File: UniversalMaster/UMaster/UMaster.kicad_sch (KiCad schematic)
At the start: 1 part, among them U1 PIC16F1789

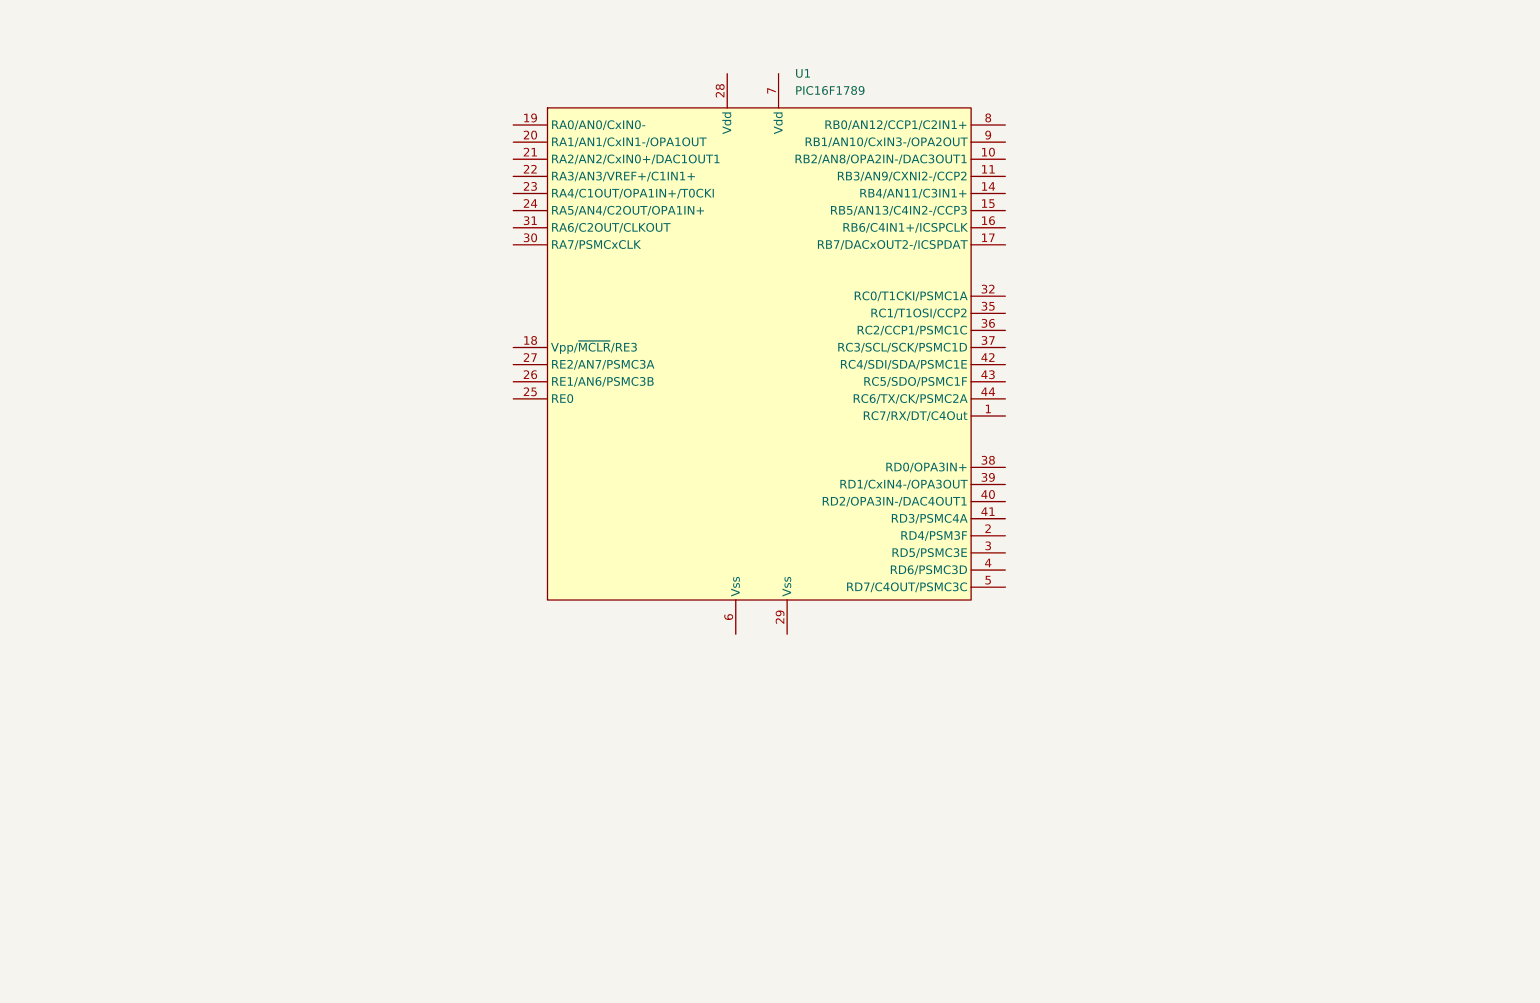
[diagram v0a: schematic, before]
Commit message: updated Universal Master schematic
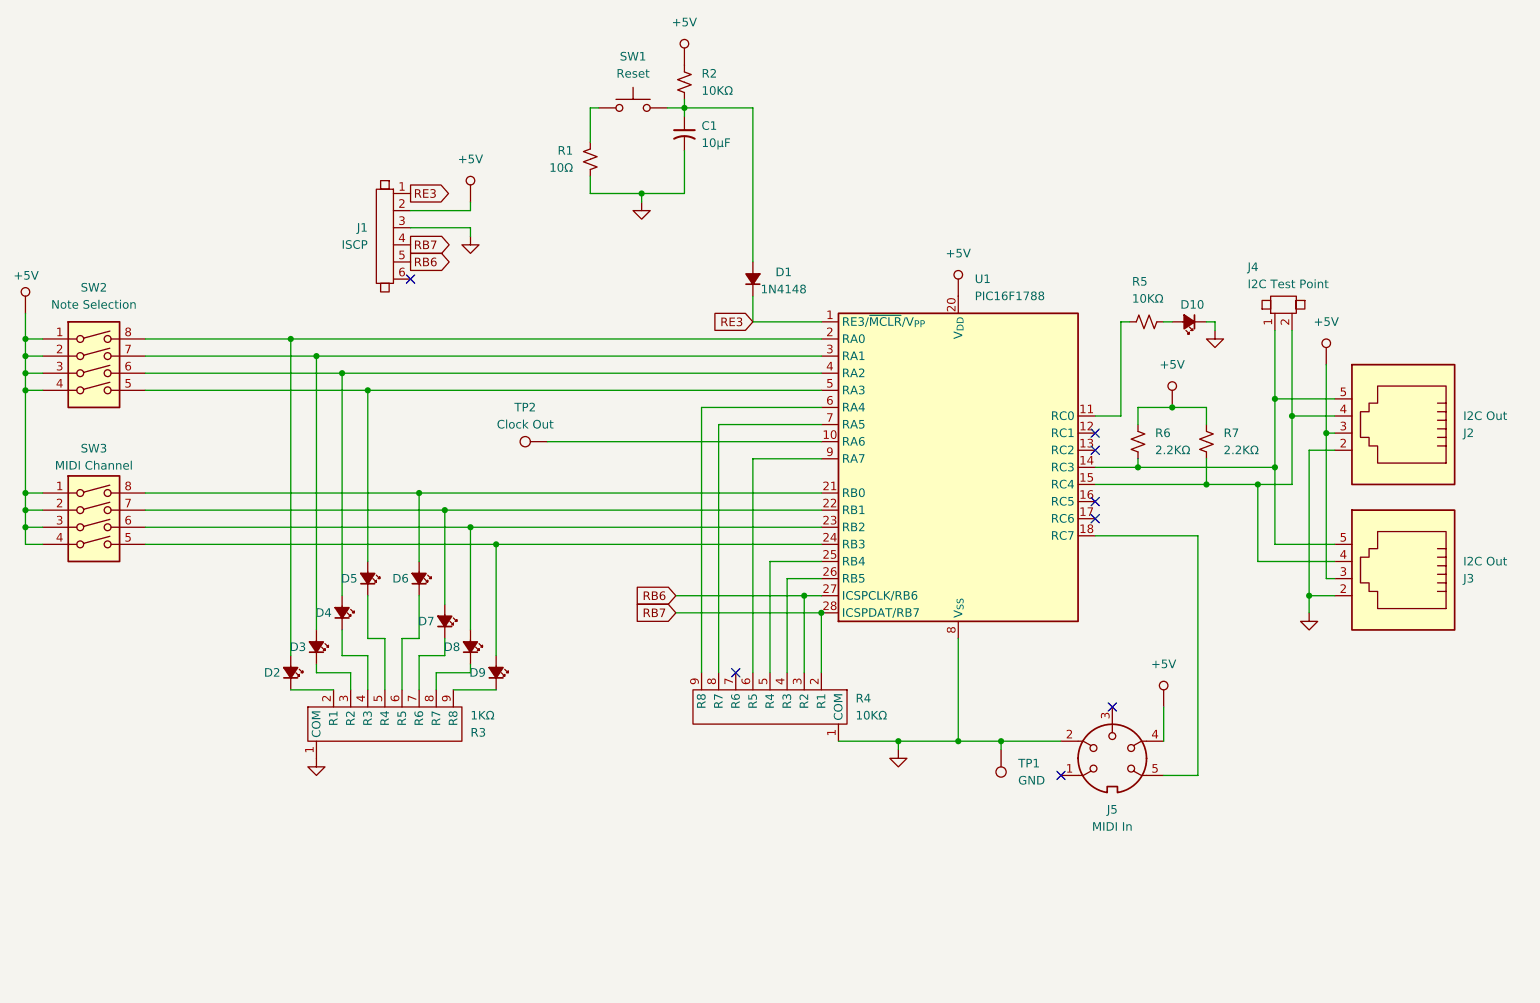
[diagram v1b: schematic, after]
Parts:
- removed U1: PIC16F1789, OF Footprints:TQFP-44_10x10mm_P0.8mm_Handsolder, symbol 2_JB_Custom_sym:PIC16F1789_44
- added C1: 10µF, symbol Device:C_Small_US
- added D1: 1N4148, 2JB_Footprints:D_0805, symbol Device:D_Small_Filled
- added D10, D2, D3, D4, D5, D6, D7, D8, D9: LED_Small_Filled, 2JB_Footprints:D_0805, symbol Device:LED_Small_Filled
- added J1: ISCP, 2JB_Footprints:1X6_100mil_Header, symbol 2_JB_Custom_sym:Jumper_6_Pin
- added J2, J3: I2C Out, 2JB_Footprints:RJ11, symbol Connector:RJ11
- added J4: I2C Test Point, 2JB_Footprints:1X2_100mil_Header, symbol 2_JB_Custom_sym:Jumper_2_Pin
- added J5: MIDI In, 2JB_Footprints:DIN-5PIN_MIDI, symbol Connector:DIN-5
- added R1: 10Ω, 2JB_Footprints:C_0805, symbol Device:R_Small_US
- added R2, R5: 10KΩ, 2JB_Footprints:C_0805, symbol Device:R_Small_US
- added R3: 1KΩ, 2JB_Footprints:1x9_100mil_Header, symbol 2_JB_Custom_sym:In-Line-R-Pack
- added R4: 10KΩ, 2JB_Footprints:1x9_100mil_Header, symbol 2_JB_Custom_sym:In-Line-R-Pack
- added R6, R7: 2.2KΩ, 2JB_Footprints:C_0805, symbol Device:R_Small_US
- added SW1: Reset, Button_Switch_THT:SW_PUSH_6mm, symbol Switch:SW_Push
- added SW2: Note Selection, Package_DIP:DIP-8_W7.62mm, symbol Switch:SW_DIP_x04
- added SW3: MIDI Channel, Package_DIP:DIP-8_W7.62mm, symbol Switch:SW_DIP_x04
- added TP1: GND, 2JB_Footprints:1X1_100mil_Header, symbol Connector:TestPoint
- added TP2: Clock Out, 2JB_Footprints:1X1_100mil_Header, symbol Connector:TestPoint
- added U1: PIC16F1788, Package_SO:SSOP-28_5.3x10.2mm_P0.65mm, symbol MCU_Microchip_PIC16:PIC16F1786-xSS
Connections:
- new net: TP2.1, U1.10 (RA6)
- new net: D4.1 (K), R3.4 (R3)
- new net: D4.2 (A), SW2.6, U1.4 (RA2)
- new net: C1.1, D1.2 (A), R2.2, SW1.2
- new net: D3.1 (K), R3.3 (R2)
- new net: D3.2 (A), SW2.7, U1.3 (RA1)
- new net: D5.1 (K), R3.5 (R4)
- new net: D5.2 (A), SW2.5, U1.5 (RA3)
- new net: SW2.1, SW2.2, SW2.3, SW2.4, SW3.1, SW3.2, SW3.3, SW3.4
- new net: D9.2 (A), SW3.5, U1.24 (RB3)
- new net: D8.2 (A), SW3.6, U1.23 (RB2)
- new net: D7.2 (A), SW3.7, U1.22 (RB1)
- new net: D6.2 (A), SW3.8, U1.21 (RB0)
- new net: D10.2 (A), R5.2
- new net: R1.1, SW1.1
- new net: J2.3, J3.3
- new net: J2.4, J3.4, J4.2, R7.2, U1.15 (RC4)
- new net: J2.5, J3.5, J4.1, R6.2, U1.14 (RC3)
- new net: R5.1, U1.11 (RC0)
- new net: J5.5, U1.18 (RC7)
- new net: D2.2 (A), SW2.8, U1.2 (RA0)
- new net: R4.5 (R4), U1.25 (RB4)
- new net: R4.4 (R3), U1.26 (RB5)
- new net: R4.9 (R8), U1.6 (RA4)
- new net: R4.8 (R7), U1.7 (RA5)
- new net: R4.6 (R5), U1.9 (RA7)
- new net: R6.1, R7.1
- new net: D9.1 (K), R3.9 (R8)
- new net: D2.1 (K), R3.2 (R1)
- new net: D6.1 (K), R3.6 (R5)
- new net: D7.1 (K), R3.7 (R6)
- new net: D8.1 (K), R3.8 (R7)
- new net GND: C1.2, D10.1 (K), J1.3, J2.2, J3.2, J5.2, R1.2, R3.1 (COM), R4.1 (COM), TP1.1, U1.19 (V_{SS}), U1.8 (V_{SS})
- new net RB6: J1.5, R4.3 (R2), U1.27 (ICSPCLK/RB6)
- new net RB7: J1.4, R4.2 (R1), U1.28 (ICSPDAT/RB7)
- new net RE3: D1.1 (K), J1.1, U1.1 (RE3/~{MCLR}/V_{PP})
- no-connect marks 0 -> 8

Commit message: made new master, pluck and fret circuits
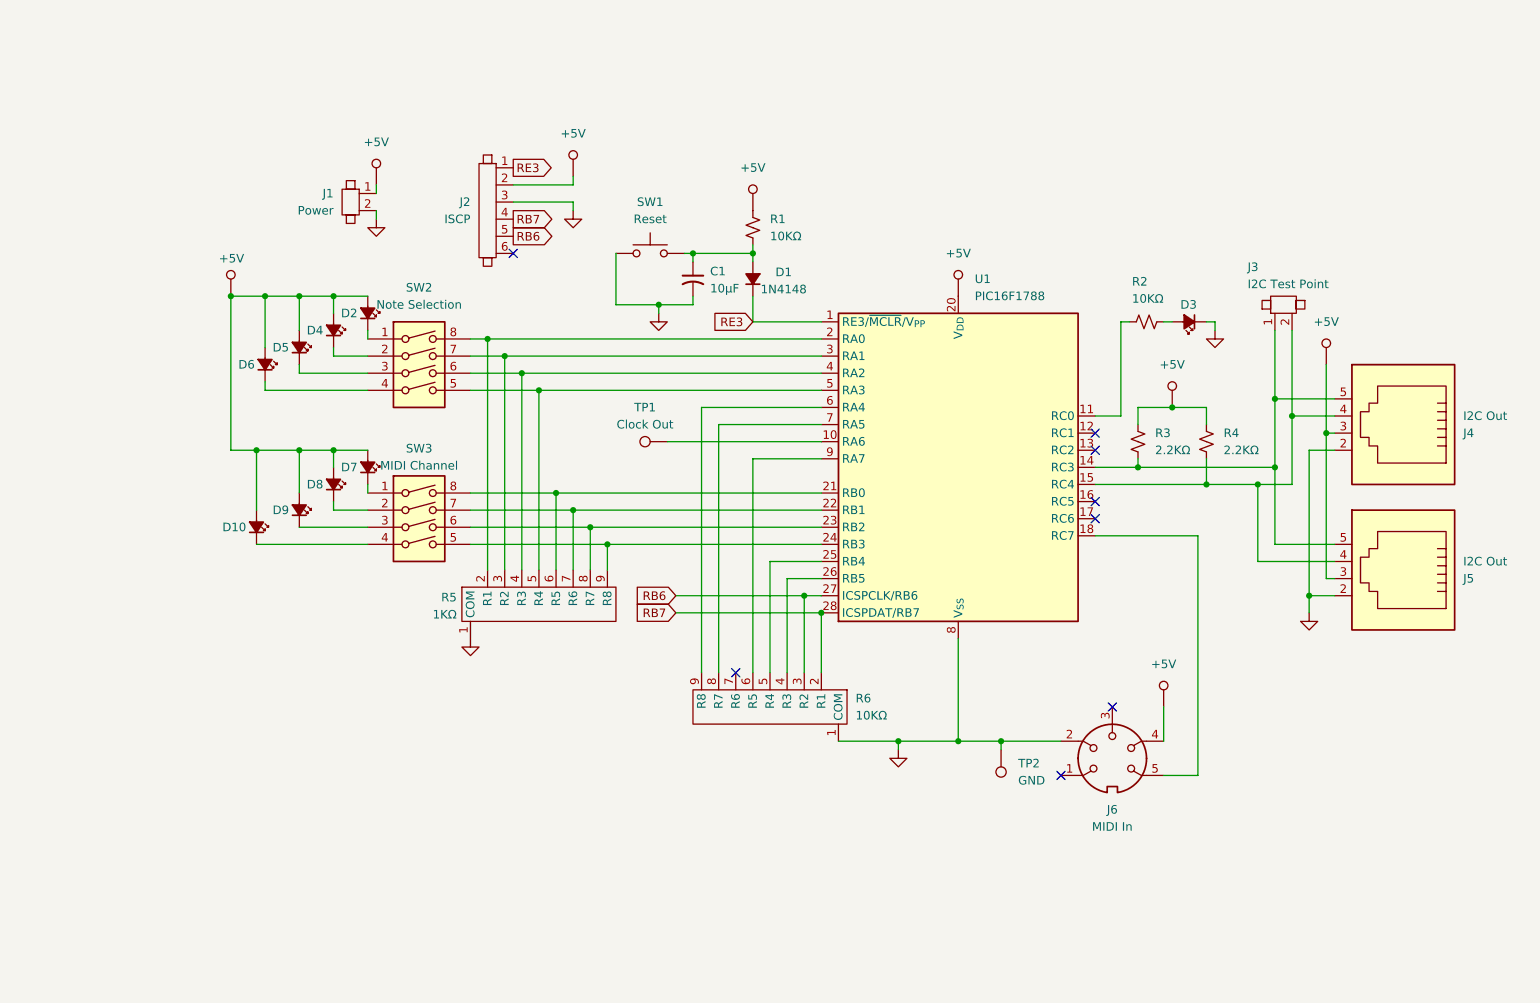
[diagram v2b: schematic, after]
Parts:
- removed R1: 10Ω, 2JB_Footprints:C_0805, symbol Device:R_Small_US
- added J1: Power, 2JB_Footprints:2PinMolex, symbol 2_JB_Custom_sym:Jumper_2_Pin
- renumbered D9 to D10, D5 to D2, D10 to D3, D3 to D5, D2 to D6, D6 to D7, D7 to D8, D8 to D9, J1 to J2, J4 to J3, J2 to J4, J3 to J5, J5 to J6, R2 to R1, R5 to R2, R6 to R3, R7 to R4, R3 to R5, R4 to R6, TP2 to TP1, TP1 to TP2
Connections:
- net GND: now also SW1.1, J1.2
- net at D4.1 (K): now also SW2.2; no longer R5.4 (R3)
- net at SW2.6, U1.4 (RA2): now also R5.4 (R3); no longer D4.2 (A)
- net at D5.1 (K): now also SW2.3; no longer R5.3 (R2)
- net at SW2.7, U1.3 (RA1): now also R5.3 (R2); no longer D5.2 (A)
- net at D2.1 (K): now also SW2.1; no longer R5.5 (R4)
- net at SW2.5, U1.5 (RA3): now also R5.5 (R4); no longer D2.2 (A)
- net at SW3.5, U1.24 (RB3): now also R5.9 (R8); no longer D10.2 (A)
- net at SW3.6, U1.23 (RB2): now also R5.8 (R7); no longer D9.2 (A)
- net at SW3.7, U1.22 (RB1): now also R5.7 (R6); no longer D8.2 (A)
- net at SW3.8, U1.21 (RB0): now also R5.6 (R5); no longer D7.2 (A)
- net at SW2.8, U1.2 (RA0): now also R5.2 (R1); no longer D6.2 (A)
- net at D10.1 (K): now also SW3.4; no longer R5.9 (R8)
- net at D6.1 (K): now also SW2.4; no longer R5.2 (R1)
- net at D7.1 (K): now also SW3.1; no longer R5.6 (R5)
- net at D8.1 (K): now also SW3.2; no longer R5.7 (R6)
- net at D9.1 (K): now also SW3.3; no longer R5.8 (R7)
- new net: D10.2 (A), D2.2 (A), D4.2 (A), D5.2 (A), D6.2 (A), D7.2 (A), D8.2 (A), D9.2 (A)
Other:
- moved on the sheet: C1, D10, D2, D4, D5, D6, D7, D8, D9, J2, R1, R5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

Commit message: designed universal PCB
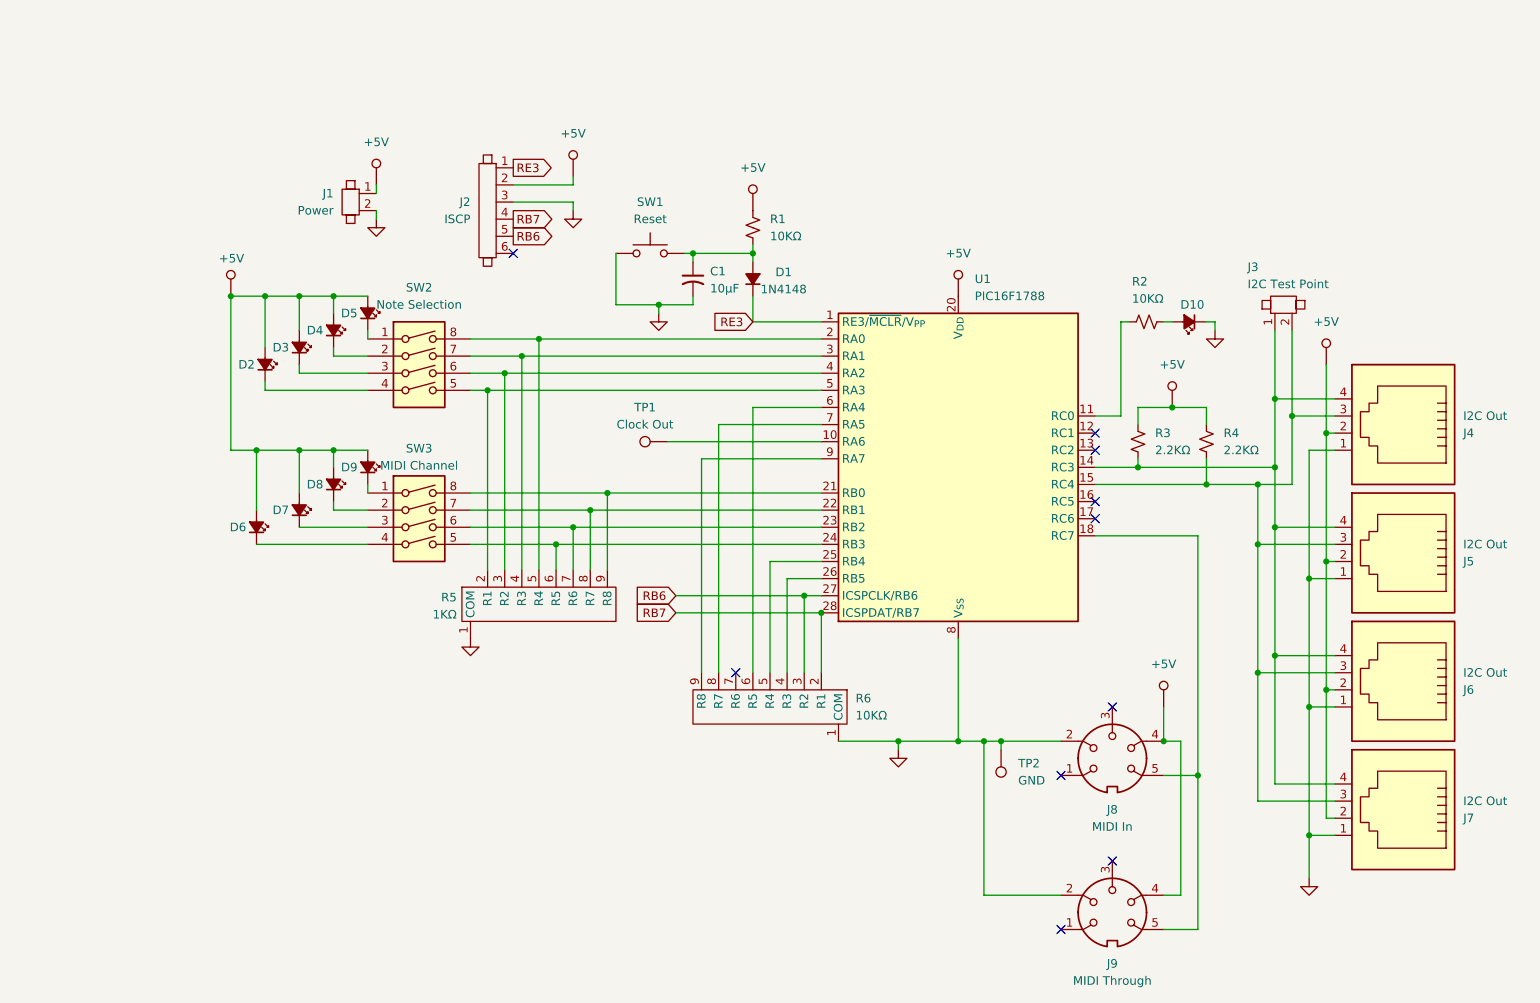
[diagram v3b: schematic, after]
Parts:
- added J6, J7: I2C Out, 2JB_Footprints:RJ11, symbol Connector:RJ11
- added J9: MIDI Through, 2JB_Footprints:DIN-5PIN_MIDI, symbol Connector:DIN-5
- C1: footprint (none) -> Capacitor_THT:C_Radial_D6.3mm_H11.0mm_P2.50mm
- U1: footprint Package_SO:SSOP-28_5.3x10.2mm_P0.65mm -> Package_DFN_QFN:QFN-28-1EP_6x6mm_P0.65mm_EP4.25x4.25mm
- renumbered D3 to D10, D6 to D2, D5 to D3, D2 to D5, D10 to D6, D9 to D7, D7 to D9, J6 to J8
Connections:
- net GND: now also J4.1, J5.1, J6.1, J7.1, J9.2; no longer J4.2, J5.2
- net at SW3.5, U1.24 (RB3): now also R5.6 (R5); no longer R5.9 (R8)
- net at SW3.6, U1.23 (RB2): now also R5.7 (R6); no longer R5.8 (R7)
- net at SW3.7, U1.22 (RB1): now also R5.8 (R7); no longer R5.7 (R6)
- net at SW3.8, U1.21 (RB0): now also R5.9 (R8); no longer R5.6 (R5)
- net at J4.3, J5.3: now also J3.2, R4.2, U1.15 (RC4), J6.3, J7.3
- net at J3.1, R3.2, U1.14 (RC3): now also J4.4, J5.4, J6.4, J7.4; no longer J4.5, J5.5
- net at J8.5, U1.18 (RC7): now also J9.5
- net at SW2.8, U1.2 (RA0): now also R5.5 (R4); no longer R5.2 (R1)
- net at SW2.7, U1.3 (RA1): now also R5.4 (R3); no longer R5.3 (R2)
- net at SW2.6, U1.4 (RA2): now also R5.3 (R2); no longer R5.4 (R3)
- net at SW2.5, U1.5 (RA3): now also R5.2 (R1); no longer R5.5 (R4)
- net at U1.6 (RA4): now also R6.6 (R5); no longer R6.9 (R8)
- net at U1.9 (RA7): now also R6.9 (R8); no longer R6.6 (R5)
- net at J8.4: now also J9.4
- new net: J4.2, J5.2, J6.2, J7.2
- no-connect marks 8 -> 10
